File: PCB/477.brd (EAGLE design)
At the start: 73.3 x 50.8 mm, 48 parts, among them IC2 STM32F407VGT6, U2 ESP8266-12E/ESP-12E, Y1 8MHz

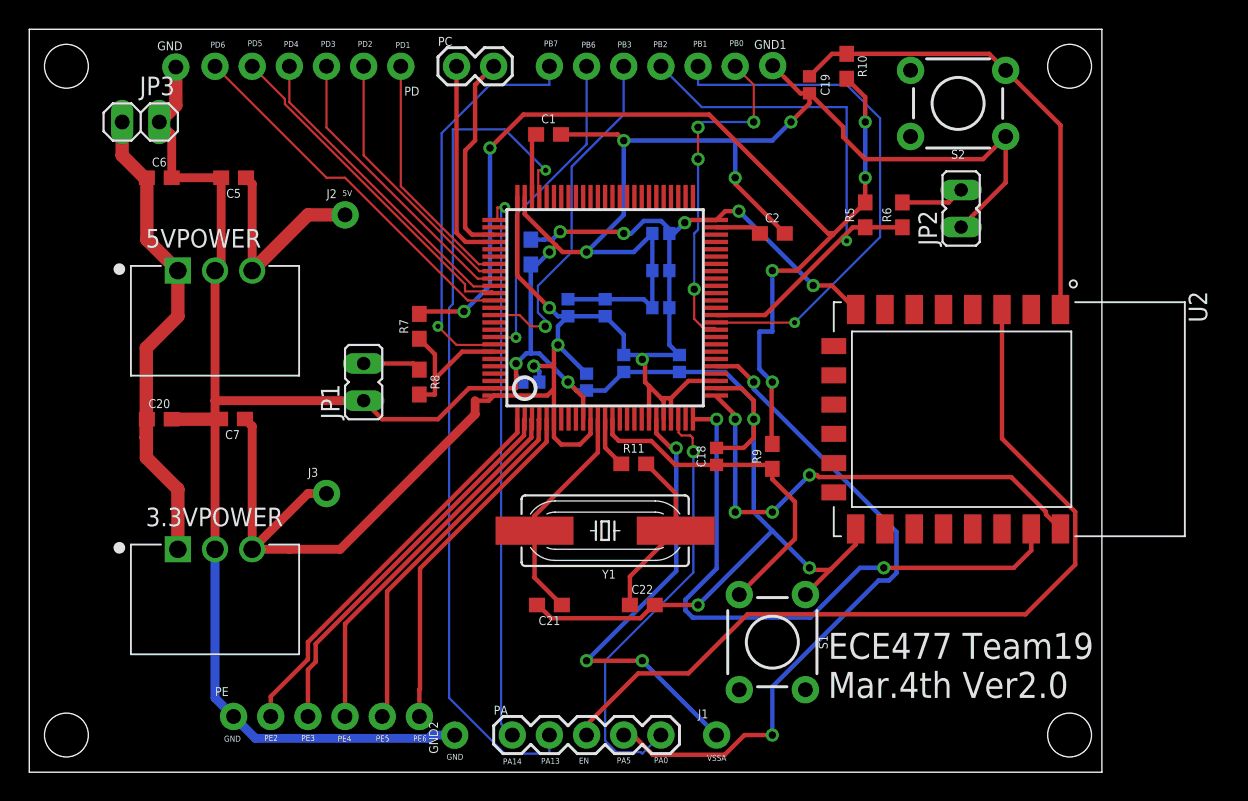
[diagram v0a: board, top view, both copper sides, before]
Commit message: Updated PCB files
Modified main PCB and added the second PCB for relay
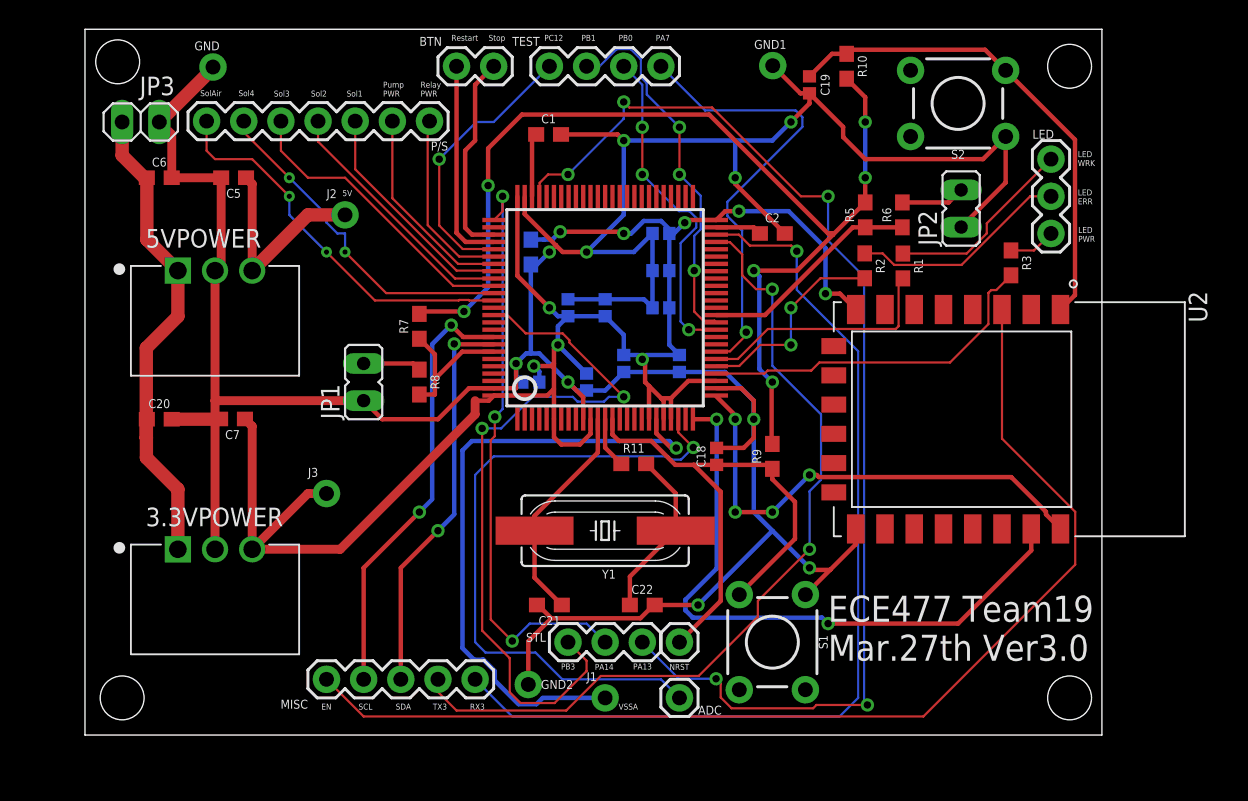
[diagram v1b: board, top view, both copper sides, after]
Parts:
- removed PA: (no value), SparkFun-Connectors:1X05
- removed PD, PE, PE1: (no value), SparkFun-Connectors:1X06_NO_SILK
- added ADC, NRST: (no value), SparkFun-Connectors:1X01
- added LED, STL: (no value), SparkFun-Connectors:1X03
- added MISC: (no value), SparkFun-Connectors:1X05
- added P/S: (no value), SparkFun-Connectors:1X07
- added R1, R2, R3: 150, SparkFun-Resistors:0603
- added TEST: (no value), SparkFun-Connectors:1X04
- moved J1 8.03 mm to (49.5, 15.2)
- moved GND2 6.11 mm to (44.3, 16.2)
- moved GND 2.54 mm to (22.7, 58.4)
- renumbered PC to BTN
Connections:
- net PA2 renamed TX2
- net PA3 renamed RX2
- net PC10 renamed B/STP
- net PC11 renamed B/RSTA
- removed net PA0: IC2.23, PA.5
- removed net PA5: IC2.30, PA.4
- removed net PB2: IC2.37, PE1.4, R5.1, R6.1
- removed net PB6: IC2.92, PE1.2
- removed net PB7: IC2.93, PE1.1
- removed net PD1: IC2.82, PD.1
- removed net PD2: IC2.83, PD.2
- removed net PD3: IC2.84, PD.3
- removed net PD4: IC2.85, PD.4
- removed net PD5: IC2.86, PD.5
- removed net PD6: IC2.87, PD.6
- removed net PE2: IC2.1, PE.2
- removed net PE3: IC2.2, PE.3
- removed net PE4: IC2.3, PE.4
- removed net PE5: IC2.4, PE.5
- removed net PE6: IC2.5, PE.6
- new net ADC: ADC.1, IC2.23
- new net BOOT1: IC2.37, R5.1, R6.1
- new net L/ERR: LED.2, R2.1
- new net L/PWR: LED.3, R3.1
- new net L/WRK: LED.1, R1.1
- new net N$1: IC2.29, R3.2
- new net N$2: IC2.30, R2.2
- new net N$4: IC2.31, R1.2
- new net P/PUMP: IC2.82, P/S.2
- new net P/RLY: IC2.81, P/S.1
- new net PA7: IC2.32, TEST.4
- new net PC12: IC2.80, TEST.1
- new net RX3: IC2.48, MISC.1
- new net SCL: IC2.92, MISC.4
- new net SDA: IC2.93, MISC.3
- new net SOL1: IC2.83, P/S.3
- new net SOL2: IC2.84, P/S.4
- new net SOL3: IC2.85, P/S.5
- new net SOL4: IC2.86, P/S.6
- new net SOLAIR: IC2.87, P/S.7
- new net TX3: IC2.47, MISC.2
- net EN: now also MISC.5; no longer PA.3
- net GND: no longer PE.1
- net NRST: now also NRST.1
- net PA13: now also STL.3; no longer PA.2
- net PA14: now also STL.2; no longer PA.1
- net PB0: now also TEST.3; no longer PE1.6
- net PB1: now also TEST.2; no longer PE1.5
- net PB3: now also STL.1; no longer PE1.3
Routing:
- net RX3: track 0.00 -> 66.0 mm, vias 0 -> 1
- net TX3: track 0.00 -> 57.5 mm, vias 0 -> 2
- net PA5: track 46.4 -> 0.00 mm, vias 2 -> 0
- net ADC: track 0.00 -> 45.2 mm, vias 0 -> 1
- net PB2: track 38.6 -> 0.00 mm, vias 1 -> 0
- net PA7: track 0.00 -> 31.2 mm, vias 0 -> 1
- net PA0: track 30.0 -> 0.00 mm, vias 1 -> 0
- net SCL: track 0.00 -> 30.0 mm, vias 0 -> 2
- net PB7: track 27.7 -> 0.00 mm, vias 1 -> 0
- net PE2: track 27.3 -> 0.00 mm
- net SDA: track 0.00 -> 27.2 mm, vias 0 -> 2
- net SOLAIR: track 0.00 -> 26.7 mm, vias 0 -> 2
- net PE3: track 26.5 -> 0.00 mm
- net PD6: track 25.7 -> 0.00 mm
- net PB3: track 24.2 -> 49.9 mm, vias 1 -> 2
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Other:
- board size 73.3 x 50.8 mm -> 69.5 x 48.2 mm
- board text added: "ECE477 Team19 Mar.27th Ver3.0"
- board text added: "LED ERR"
- board text added: "LED PWR"
- board text added: "LED WRK"
- board text added: "NRST"
- board text added: "PA7"
- board text added: "PC12"
- board text added: "Pump PWR"
- board text added: "RX3"
- board text added: "Relay PWR"
- board text added: "Restart"
- board text added: "SCL"
- board text added: "SDA"
- board text added: "Sol1"
- board text added: "Sol2"
- board text added: "Sol3"
- board text added: "Sol4"
- board text added: "SolAir"
- board text added: "Stop"
- board text added: "TX3"
- board text removed: "ECE477 Team19 Mar.4th Ver2.0"
- board text removed: "GND"
- board text removed: "PA0"
- board text removed: "PA5"
- board text removed: "PB2"
- board text removed: "PB6"
- board text removed: "PB7"
- board text removed: "PD1"
- board text removed: "PD2"
- board text removed: "PD3"
- board text removed: "PD4"
- board text removed: "PD5"
- board text removed: "PD6"
- board text removed: "PE2"
- board text removed: "PE3"
- board text removed: "PE4"
- board text removed: "PE5"
- board text removed: "PE6"
